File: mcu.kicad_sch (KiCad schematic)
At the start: 39 parts, among them J10 BuzzerHV, J11 BuzzerLV, J6 JST_06, J7 SPI_DBG, J8 MTRBTN, J9 Bluetooth, Q4 MMBTA42, U7 STM32F103C8Tx

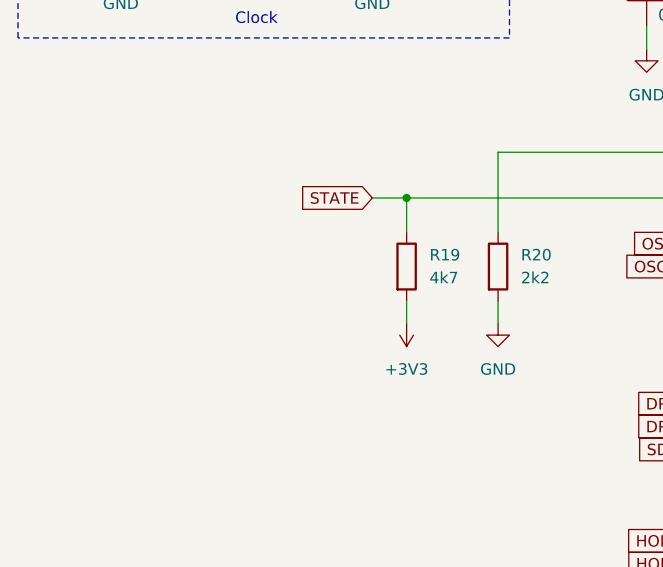
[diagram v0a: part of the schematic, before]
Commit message: Fix pullup IMU, pulldown boot0, vbat before resi
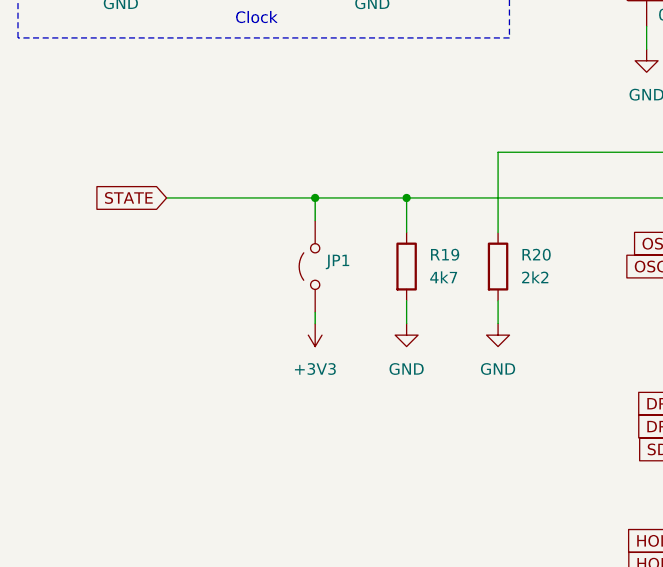
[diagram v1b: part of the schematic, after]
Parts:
- added JP1: ~, symbol Jumper:Jumper_2_Open
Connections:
- net +3V3: now also JP1.1 (A); no longer R19.2
- net GND: now also R19.2
- net STATE: now also JP1.2 (B)
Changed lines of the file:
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@@
 	)
 	(junction
+		(at 50.8 68.58)
+		(diameter 0)
+		(color 0 0 0 0)
+	)
+	(junction
 		(at 205.74 21.59)
 		(diameter 0)
@@
 	(wire
 		(pts
+			(xy 50.8 68.58) (xy 50.8 71.12)
+		)
+		(stroke
+			(width 0)
+			(type default)
+		)
+	)
+	(wire
+		(pts
 			(xy 243.84 59.69) (xy 247.65 59.69)
 		)
@@
 	(wire
 		(pts
+			(xy 50.8 68.58) (xy 60.96 68.58)
+		)
+		(stroke
+			(width 0)
+			(type default)
+		)
+	)
+	(wire
+		(pts
 			(xy 29.21 27.94) (xy 29.21 31.75)
 		)
@@
 	(wire
 		(pts
+			(xy 50.8 81.28) (xy 50.8 82.55)
+		)
+		(stroke
+			(width 0)
+			(type default)
+		)
+	)
+	(wire
+		(pts
 			(xy 204.47 58.42) (xy 217.17 58.42)
 		)
@@
 	(wire
 		(pts
-			(xy 57.15 68.58) (xy 60.96 68.58)
+			(xy 34.29 68.58) (xy 50.8 68.58)
 		)
 		(stroke
@@
 	(global_label "STATE"
 		(shape input)
-		(at 57.15 68.58 180)
+		(at 34.29 68.58 180)
 		(fields_autoplaced yes)
 		(effects
@@
 		)
 		(property "Intersheetrefs" "${INTERSHEET_REFS}"
-			(at 48.7825 68.58 0)
+			(at 25.9225 68.58 0)
 			(effects
 				(font
@@
 	)
 	(symbol
+		(lib_id "power:GND")
+		(at 60.96 82.55 0)
+		(unit 1)
+		(exclude_from_sim no)
+		(in_bom yes)
+		(on_board yes)
+		(dnp no)
+		(property "Reference" "#PWR042"
+			(at 60.96 88.9 0)
+			(effects
+				(font
+					(size 1.27 1.27)
+				)
+				(hide yes)
+			)
+		)
+		(property "Value" "GND"
+			(at 60.96 87.63 0)
+			(effects
+				(font
+					(size 1.27 1.27)
+				)
+			)
+		)
+		(property "Footprint" ""
+			(at 60.96 82.55 0)
+			(effects
+				(font
+					(size 1.27 1.27)
+				)
+				(hide yes)
+			)
+		)
+		(property "Datasheet" ""
+			(at 60.96 82.55 0)
+			(effects
+				(font
+					(size 1.27 1.27)
+				)
+				(hide yes)
+			)
+		)
+		(property "Description" ""
+			(at 60.96 82.55 0)
+			(effects
+				(font
+					(size 1.27 1.27)
+				)
+				(hide yes)
+			)
+		)
+		(pin "1"
+		)
+		(instances
+			(project "ShiftWay_f103"
+				(path "/c57bc97c-1c43-4bb1-9424-fed846030b7b/013bb254-f239-4c32-8f76-0a97895c10b6"
+					(reference "#PWR042")
+					(unit 1)
+				)
+			)
+		)
+	)
+	(symbol
 		(lib_id "Device:C")
 		(at 29.21 35.56 0)
@@
 	)
 	(symbol
+		(lib_id "Jumper:Jumper_2_Open")
+		(at 50.8 76.2 90)
+		(unit 1)
+		(exclude_from_sim yes)
+		(in_bom yes)
+		(on_board yes)
+		(dnp no)
+		(fields_autoplaced yes)
+		(property "Reference" "JP1"
+			(at 52.07 75.5649 90)
+			(effects
+				(font
+					(size 1.27 1.27)
+				)
+				(justify right)
+			)
+		)
+		(property "Value" "~"
+			(at 52.07 77.47 90)
+			(effects
+				(font
+					(size 1.27 1.27)
+				)
+				(justify right)
+			)
+		)
+		(property "Footprint" ""
+			(at 50.8 76.2 0)
+			(effects
+				(font
+					(size 1.27 1.27)
+				)
+				(hide yes)
+			)
+		)
+		(property "Datasheet" "~"
+			(at 50.8 76.2 0)
+			(effects
+				(font
+					(size 1.27 1.27)
+				)
+				(hide yes)
+			)
+		)
+		(property "Description" "Jumper, 2-pole, open"
+			(at 50.8 76.2 0)
+			(effects
+				(font
+					(size 1.27 1.27)
+				)
+				(hide yes)
+			)
+		)
+		(pin "2"
+		)
+		(pin "1"
+		)
+		(instances
+			(project "ShiftWay_f103"
+				(path "/c57bc97c-1c43-4bb1-9424-fed846030b7b/013bb254-f239-4c32-8f76-0a97895c10b6"
+					(reference "JP1")
+					(unit 1)
+				)
+			)
+		)
+	)
+	(symbol
 		(lib_id "power:GND")
 		(at 232.41 151.13 0)
@@
 	)
 	(symbol
+		(lib_id "power:+3V3")
+		(at 50.8 82.55 180)
+		(unit 1)
+		(exclude_from_sim no)
+		(in_bom yes)
+		(on_board yes)
+		(dnp no)
+		(fields_autoplaced yes)
+		(property "Reference" "#PWR0105"
+			(at 50.8 78.74 0)
+			(effects
+				(font
+					(size 1.27 1.27)
+				)
+				(hide yes)
+			)
+		)
+		(property "Value" "+3V3"
+			(at 50.8 87.63 0)
+			(effects
+				(font
+					(size 1.27 1.27)
+				)
+			)
+		)
+		(property "Footprint" ""
+			(at 50.8 82.55 0)
+			(effects
+				(font
+					(size 1.27 1.27)
+				)
+				(hide yes)
+			)
+		)
+		(property "Datasheet" ""
+			(at 50.8 82.55 0)
+			(effects
+				(font
+					(size 1.27 1.27)
+				)
+				(hide yes)
+			)
+		)
+		(property "Description" ""
+			(at 50.8 82.55 0)
+			(effects
+				(font
+					(size 1.27 1.27)
+				)
+				(hide yes)
+			)
+		)
+		(pin "1"
+		)
+		(instances
+			(project "ShiftWay_f103"
+				(path "/c57bc97c-1c43-4bb1-9424-fed846030b7b/013bb254-f239-4c32-8f76-0a97895c10b6"
+					(reference "#PWR0105")
+					(unit 1)
+				)
+			)
+		)
+	)
+	(symbol
 		(lib_id "Device:C")
 		(at 240.03 154.94 0)
@@
 					(unit 1)
 				)
-			)
-		)
-	)
-	(symbol
-		(lib_id "power:+3V3")
-		(at 60.96 82.55 180)
-		(unit 1)
-		(exclude_from_sim no)
-		(in_bom yes)
-		(on_board yes)
-		(dnp no)
-		(fields_autoplaced yes)
-		(property "Reference" "#PWR042"
-			(at 60.96 78.74 0)
-			(effects
-				(font
-					(size 1.27 1.27)
-				)
-				(hide yes)
-			)
-		)
-		(property "Value" "+3V3"
-			(at 60.96 87.63 0)
-			(effects
-				(font
-					(size 1.27 1.27)
-				)
-			)
-		)
-		(property "Footprint" ""
-			(at 60.96 82.55 0)
-			(effects
-				(font
-					(size 1.27 1.27)
-				)
-				(hide yes)
-			)
-		)
-		(property "Datasheet" ""
-			(at 60.96 82.55 0)
-			(effects
-				(font
-					(size 1.27 1.27)
-				)
-				(hide yes)
-			)
-		)
-		(property "Description" ""
-			(at 60.96 82.55 0)
-			(effects
-				(font
-					(size 1.27 1.27)
-				)
-				(hide yes)
-			)
-		)
-		(pin "1"
-		)
-		(instances
-			(project "ShiftWay_f103"
-				(path "/c57bc97c-1c43-4bb1-9424-fed846030b7b/013bb254-f239-4c32-8f76-0a97895c10b6"
-					(reference "#PWR042")
-					(unit 1)
-				)
